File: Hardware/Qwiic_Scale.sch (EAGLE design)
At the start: 32 parts, among them J1 CAP, J2 Qwiic, J3 PTH, J4 Qwiic, J7 Spring Terminal, U1 NAU7802

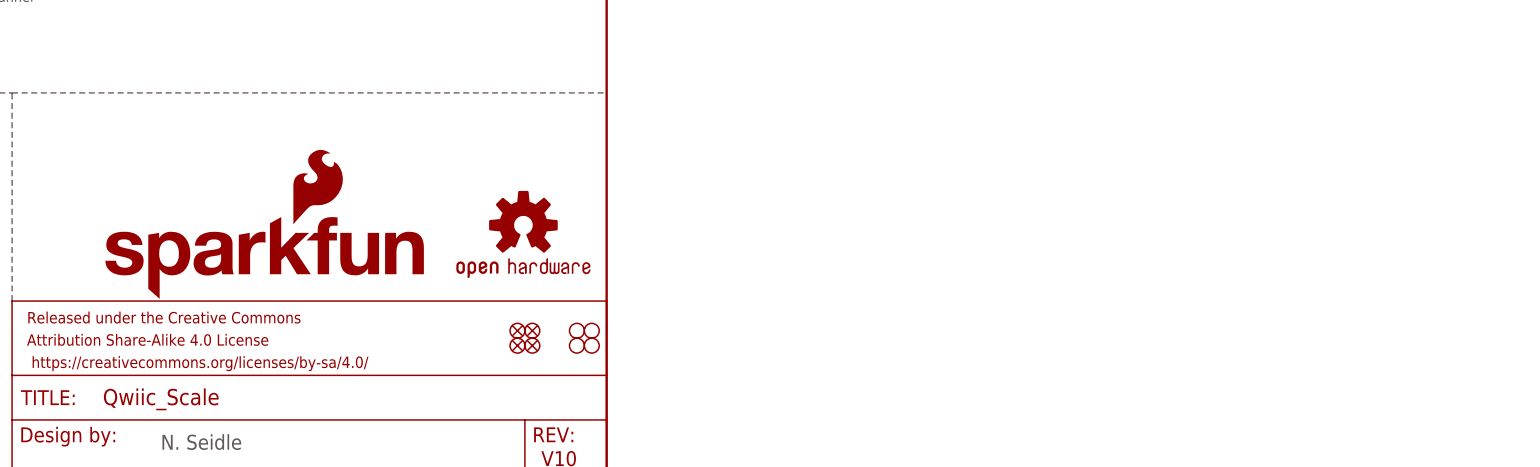
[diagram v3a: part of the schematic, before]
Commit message: Update Qwiic logo. Remove old panel files.
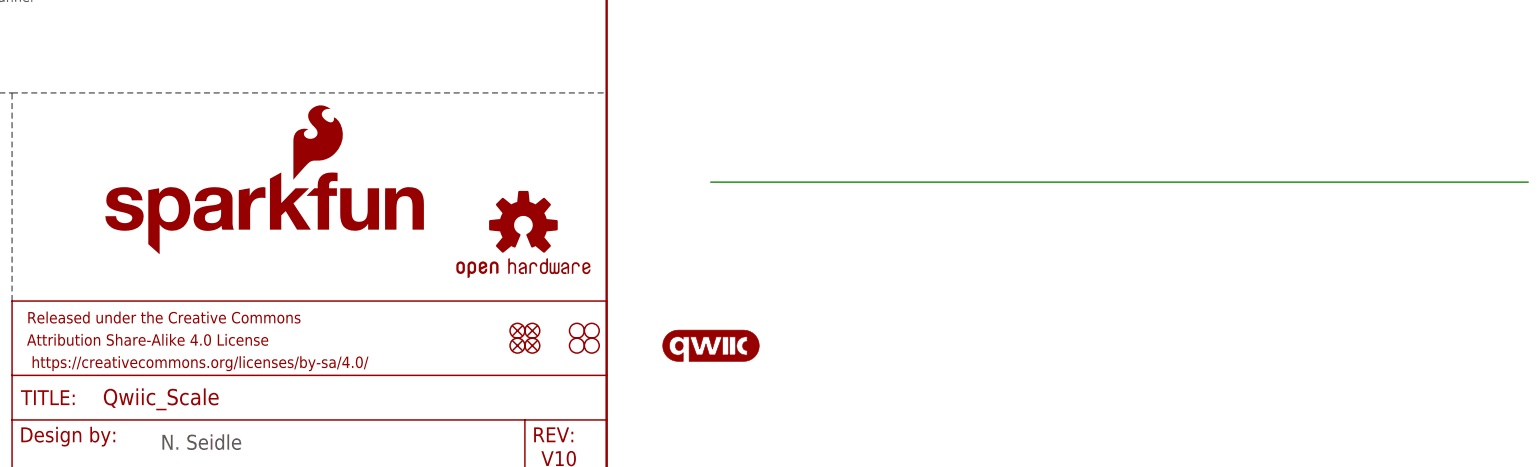
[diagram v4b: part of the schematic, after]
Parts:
- added U$26: QWIIC_LOGO_8MM, Qwiic_Logo:QWIIC_LOGO_8MM
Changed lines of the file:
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@@
 <grid distance="0.1" unitdist="inch" unit="inch" style="lines" multiple="1" display="no" altdistance="0.01" altunitdist="inch" altunit="inch"/>
 <layers>
-<layer number="1" name="Top" color="4" fill="1" visible="no" active="no"/>
-<layer number="2" name="Route2" color="1" fill="3" visible="no" active="no"/>
-<layer number="3" name="Route3" color="4" fill="3" visible="no" active="no"/>
-<layer number="4" name="Route4" color="1" fill="4" visible="no" active="no"/>
-<layer number="5" name="Route5" color="4" fill="4" visible="no" active="no"/>
-<layer number="6" name="Route6" color="1" fill="8" visible="no" active="no"/>
-<layer number="7" name="Route7" color="4" fill="8" visible="no" active="no"/>
-<layer number="8" name="Route8" color="1" fill="2" visible="no" active="no"/>
-<layer number="9" name="Route9" color="4" fill="2" visible="no" active="no"/>
-<layer number="10" name="Route10" color="1" fill="7" visible="no" active="no"/>
-<layer number="11" name="Route11" color="4" fill="7" visible="no" active="no"/>
-<layer number="12" name="Route12" color="1" fill="5" visible="no" active="no"/>
-<layer number="13" name="Route13" color="4" fill="5" visible="no" active="no"/>
-<layer number="14" name="Route14" color="1" fill="6" visible="no" active="no"/>
-<layer number="15" name="Route15" color="4" fill="6" visible="no" active="no"/>
-<layer number="16" name="Bottom" color="1" fill="1" visible="no" active="no"/>
-<layer number="17" name="Pads" color="2" fill="1" visible="no" active="no"/>
-<layer number="18" name="Vias" color="2" fill="1" visible="no" active="no"/>
-<layer number="19" name="Unrouted" color="6" fill="1" visible="no" active="no"/>
-<layer number="20" name="Dimension" color="24" fill="1" visible="no" active="no"/>
-<layer number="21" name="tPlace" color="16" fill="1" visible="no" active="no"/>
-<layer number="22" name="bPlace" color="14" fill="1" visible="no" active="no"/>
-<layer number="23" name="tOrigins" color="15" fill="1" visible="no" active="no"/>
-<layer number="24" name="bOrigins" color="15" fill="1" visible="no" active="no"/>
-<layer number="25" name="tNames" color="7" fill="1" visible="no" active="no"/>
-<layer number="26" name="bNames" color="7" fill="1" visible="no" active="no"/>
-<layer number="27" name="tValues" color="7" fill="1" visible="no" active="no"/>
-<layer number="28" name="bValues" color="7" fill="1" visible="no" active="no"/>
+<layer number="1" name="Top" color="4" fill="1" visible="yes" active="no"/>
+<layer number="2" name="Route2" color="1" fill="3" visible="yes" active="no"/>
+<layer number="3" name="Route3" color="4" fill="3" visible="yes" active="no"/>
+<layer number="4" name="Route4" color="1" fill="4" visible="yes" active="no"/>
+<layer number="5" name="Route5" color="4" fill="4" visible="yes" active="no"/>
+<layer number="6" name="Route6" color="1" fill="8" visible="yes" active="no"/>
+<layer number="7" name="Route7" color="4" fill="8" visible="yes" active="no"/>
+<layer number="8" name="Route8" color="1" fill="2" visible="yes" active="no"/>
+<layer number="9" name="Route9" color="4" fill="2" visible="yes" active="no"/>
+<layer number="10" name="Route10" color="1" fill="7" visible="yes" active="no"/>
+<layer number="11" name="Route11" color="4" fill="7" visible="yes" active="no"/>
+<layer number="12" name="Route12" color="1" fill="5" visible="yes" active="no"/>
+<layer number="13" name="Route13" color="4" fill="5" visible="yes" active="no"/>
+<layer number="14" name="Route14" color="1" fill="6" visible="yes" active="no"/>
+<layer number="15" name="Route15" color="4" fill="6" visible="yes" active="no"/>
+<layer number="16" name="Bottom" color="1" fill="1" visible="yes" active="no"/>
+<layer number="17" name="Pads" color="2" fill="1" visible="yes" active="no"/>
+<layer number="18" name="Vias" color="2" fill="1" visible="yes" active="no"/>
+<layer number="19" name="Unrouted" color="6" fill="1" visible="yes" active="no"/>
+<layer number="20" name="Dimension" color="24" fill="1" visible="yes" active="no"/>
+<layer number="21" name="tPlace" color="16" fill="1" visible="yes" active="no"/>
+<layer number="22" name="bPlace" color="14" fill="1" visible="yes" active="no"/>
+<layer number="23" name="tOrigins" color="15" fill="1" visible="yes" active="no"/>
+<layer number="24" name="bOrigins" color="15" fill="1" visible="yes" active="no"/>
+<layer number="25" name="tNames" color="7" fill="1" visible="yes" active="no"/>
+<layer number="26" name="bNames" color="7" fill="1" visible="yes" active="no"/>
+<layer number="27" name="tValues" color="7" fill="1" visible="yes" active="no"/>
+<layer number="28" name="bValues" color="7" fill="1" visible="yes" active="no"/>
 <layer number="29" name="tStop" color="7" fill="3" visible="no" active="no"/>
 <layer number="30" name="bStop" color="7" fill="6" visible="no" active="no"/>
@@
 <layer number="35" name="tGlue" color="7" fill="4" visible="no" active="no"/>
 <layer number="36" name="bGlue" color="7" fill="5" visible="no" active="no"/>
-<layer number="37" name="tTest" color="7" fill="1" visible="no" active="no"/>
-<layer number="38" name="bTest" color="7" fill="1" visible="no" active="no"/>
+<layer number="37" name="tTest" color="7" fill="1" visible="yes" active="no"/>
+<layer number="38" name="bTest" color="7" fill="1" visible="yes" active="no"/>
 <layer number="39" name="tKeepout" color="4" fill="11" visible="no" active="no"/>
 <layer number="40" name="bKeepout" color="1" fill="11" visible="no" active="no"/>
@@
 <layer number="44" name="Drills" color="7" fill="1" visible="no" active="no"/>
 <layer number="45" name="Holes" color="7" fill="1" visible="no" active="no"/>
-<layer number="46" name="Milling" color="3" fill="1" visible="no" active="no"/>
-<layer number="47" name="Measures" color="7" fill="1" visible="no" active="no"/>
-<layer number="48" name="Document" color="7" fill="1" visible="no" active="no"/>
-<layer number="49" name="Reference" color="7" fill="1" visible="no" active="no"/>
-<layer number="50" name="dxf" color="7" fill="1" visible="no" active="no"/>
-<layer number="51" name="tDocu" color="6" fill="1" visible="no" active="no"/>
-<layer number="52" name="bDocu" color="7" fill="1" visible="no" active="no"/>
-<layer number="53" name="tGND_GNDA" color="7" fill="9" visible="no" active="no"/>
-<layer number="54" name="bGND_GNDA" color="1" fill="9" visible="no" active="no"/>
-<layer number="56" name="wert" color="7" fill="1" visible="no" active="no"/>
-<layer number="57" name="tCAD" color="7" fill="1" visible="no" active="no"/>
-<layer number="59" name="tCarbon" color="7" fill="1" visible="no" active="no"/>
-<layer number="60" name="bCarbon" color="7" fill="1" visible="no" active="no"/>
+<layer number="46" name="Milling" color="3" fill="1" visible="yes" active="no"/>
+<layer number="47" name="Measures" color="7" fill="1" visible="yes" active="no"/>
+<layer number="48" name="Document" color="7" fill="1" visible="yes" active="no"/>
+<layer number="49" name="Reference" color="7" fill="1" visible="yes" active="no"/>
+<layer number="50" name="dxf" color="7" fill="1" visible="yes" active="no"/>
+<layer number="51" name="tDocu" color="6" fill="1" visible="yes" active="no"/>
+<layer number="52" name="bDocu" color="7" fill="1" visible="yes" active="no"/>
+<layer number="53" name="tGND_GNDA" color="7" fill="9" visible="yes" active="no"/>
+<layer number="54" name="bGND_GNDA" color="1" fill="9" visible="yes" active="no"/>
+<layer number="56" name="wert" color="7" fill="1" visible="yes" active="no"/>
+<layer number="57" name="tCAD" color="7" fill="1" visible="yes" active="no"/>
+<layer number="59" name="tCarbon" color="7" fill="1" visible="yes" active="no"/>
+<layer number="60" name="bCarbon" color="7" fill="1" visible="yes" active="no"/>
 <layer number="88" name="SimResults" color="9" fill="1" visible="yes" active="yes"/>
 <layer number="89" name="SimProbes" color="9" fill="1" visible="yes" active="yes"/>
@@
 <part name="R3" library="SparkFun-Resistors" deviceset="2.2KOHM" device="-0603-1/10W-1%" value="2.2k"/>
 <part name="J7" library="SparkFun-Connectors" deviceset="CONN_04" device="SPRING" value="Spring Terminal"/>
+<part name="U$26" library="Qwiic_Logo" deviceset="QWIIC_LOGO" device="_8MM" value="QWIIC_LOGO_8MM"/>
 </parts>
 <sheets>
@@
 <attribute name="VALUE" x="127" y="48.514" size="1.778" layer="96" font="vector" align="bottom-center"/>
 </instance>
-<instance part="LOGO2" gate="G$1" x="162.56" y="35.56" smashed="yes"/>
+<instance part="LOGO2" gate="G$1" x="162.56" y="43.18" smashed="yes"/>
 <instance part="GND9" gate="1" x="66.04" y="111.76" smashed="yes">
 <attribute name="VALUE" x="63.5" y="109.22" size="1.778" layer="96" font="vector"/>
@@
 <attribute name="NAME" x="53.34" y="144.272" size="1.778" layer="95" font="vector" rot="MR180"/>
 </instance>
+<instance part="U$26" gate="G$1" x="266.7" y="27.94" smashed="yes"/>
 </instances>
 <busses>
@@
 </segment>
 </net>
+<net name="N$4" class="0">
+<segment>
+<wire x1="266.7" y1="55.88" x2="406.4" y2="55.88" width="0.1524" layer="91"/>
+</segment>
+</net>
